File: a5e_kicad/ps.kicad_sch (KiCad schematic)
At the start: 48 parts

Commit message: route more rgmii io
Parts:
- C122: footprint Capacitor_SMD:C_0402_1005Metric -> Capacitor_SMD:C_0201_0603Metric
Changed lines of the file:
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@@
 			)
 		)
-		(property "Footprint" "Capacitor_SMD:C_0402_1005Metric"
+		(property "Footprint" "Capacitor_SMD:C_0201_0603Metric"
 			(at 108.9152 181.61 0)
 			(hide yes)

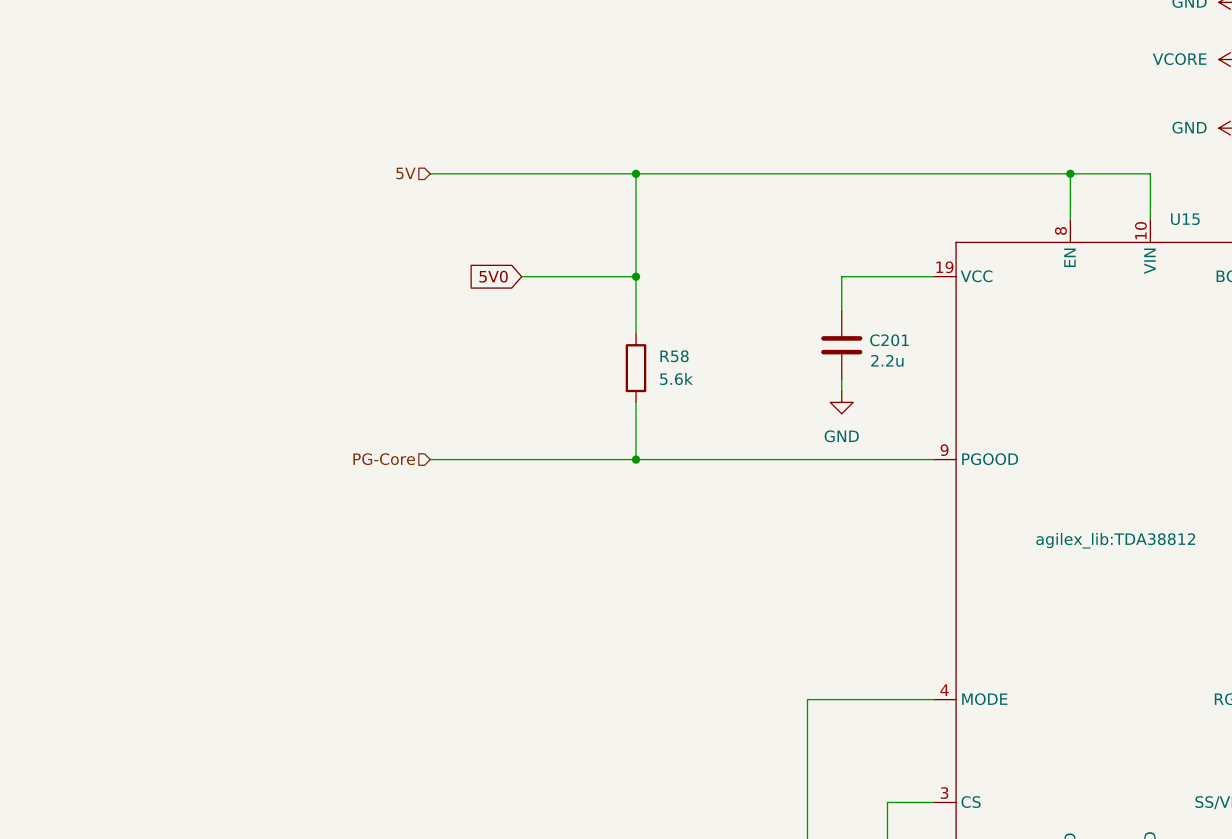
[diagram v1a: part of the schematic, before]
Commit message: add oscillator footprint and start adding ac biasing for lpddr clock
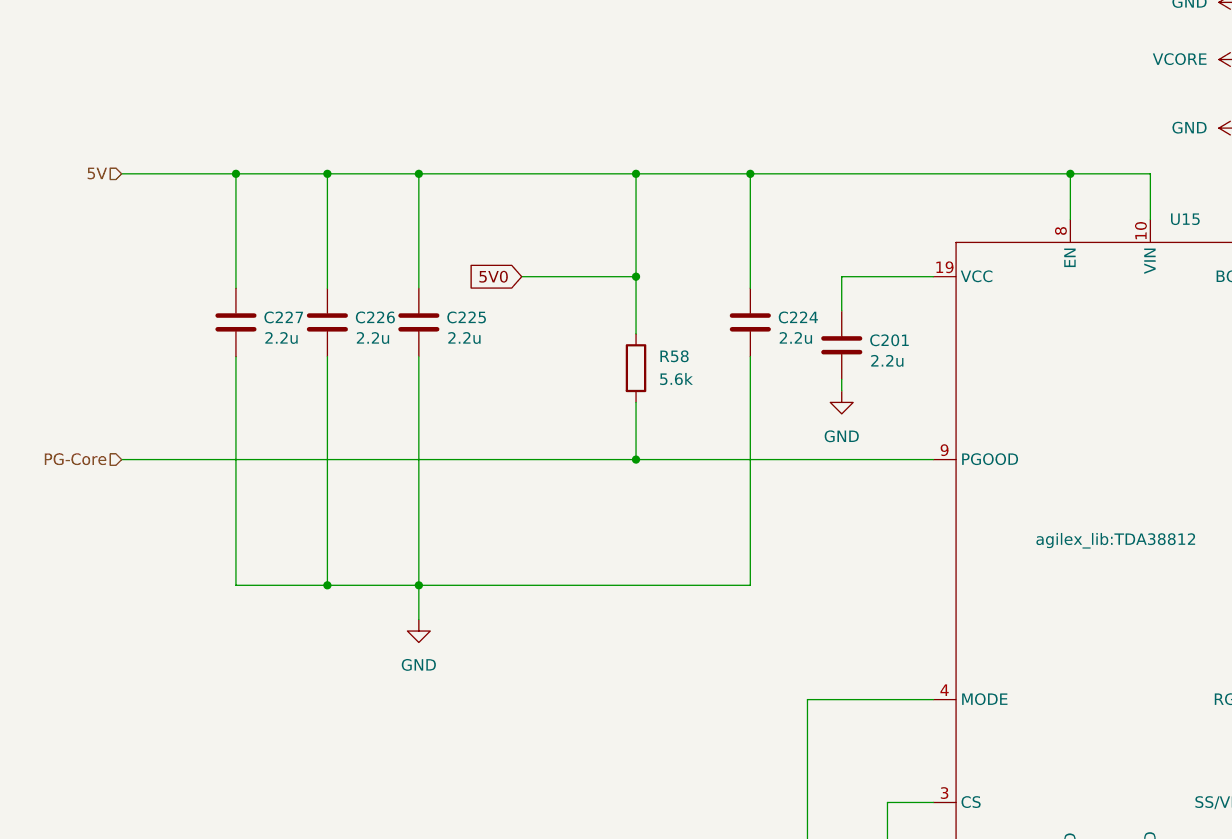
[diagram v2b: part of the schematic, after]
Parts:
- added C224, C225, C226, C227: 2.2u, Capacitor_SMD:C_0402_1005Metric, symbol Device:C
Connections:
- net 5V0: now also C224.2, C225.2, C226.2, C227.2
- net GND: now also C224.1, C225.1, C226.1, C227.1

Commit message: add 1v2 flood
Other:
- note added: "not relevant for this power"
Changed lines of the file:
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@@
 		(rev "0.1")
+	)
+	(text "not relevant for this power"
+		(exclude_from_sim no)
+		(at 234.95 138.938 0)
+		(effects
+			(font
+				(size 1.27 1.27)
+			)
+		)
 	)
 	(text "Iout = 12A, FSW = 1500Khz, VIN = 5V"

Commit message: remove extra components and make 1v8 plane
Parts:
- removed C125, C127, C128: 22U 6V3, Capacitor_SMD:C_0402_1005Metric, symbol Device:C
- removed C126: GRM32ER71A476KE15L 47uF 2mR, Capacitor_SMD:C_1210_3225Metric, symbol Device:C
